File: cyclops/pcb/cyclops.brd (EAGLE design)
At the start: 124.5 x 79.9 mm, 178 parts, among them Q4 IRF510, U1 MCP4921, U11 THS4281, U12 MAX4564, U13 ZXTD, U14 ZXTD, U15 OPA1664, U2 LT1931, U3 LT1764A, U31 TPS62153, U4 BD60HC5WEFJ, U5 TPS72325, U6 LT1711, U7 TLV3701, U8 ADR03, U9 LT1880

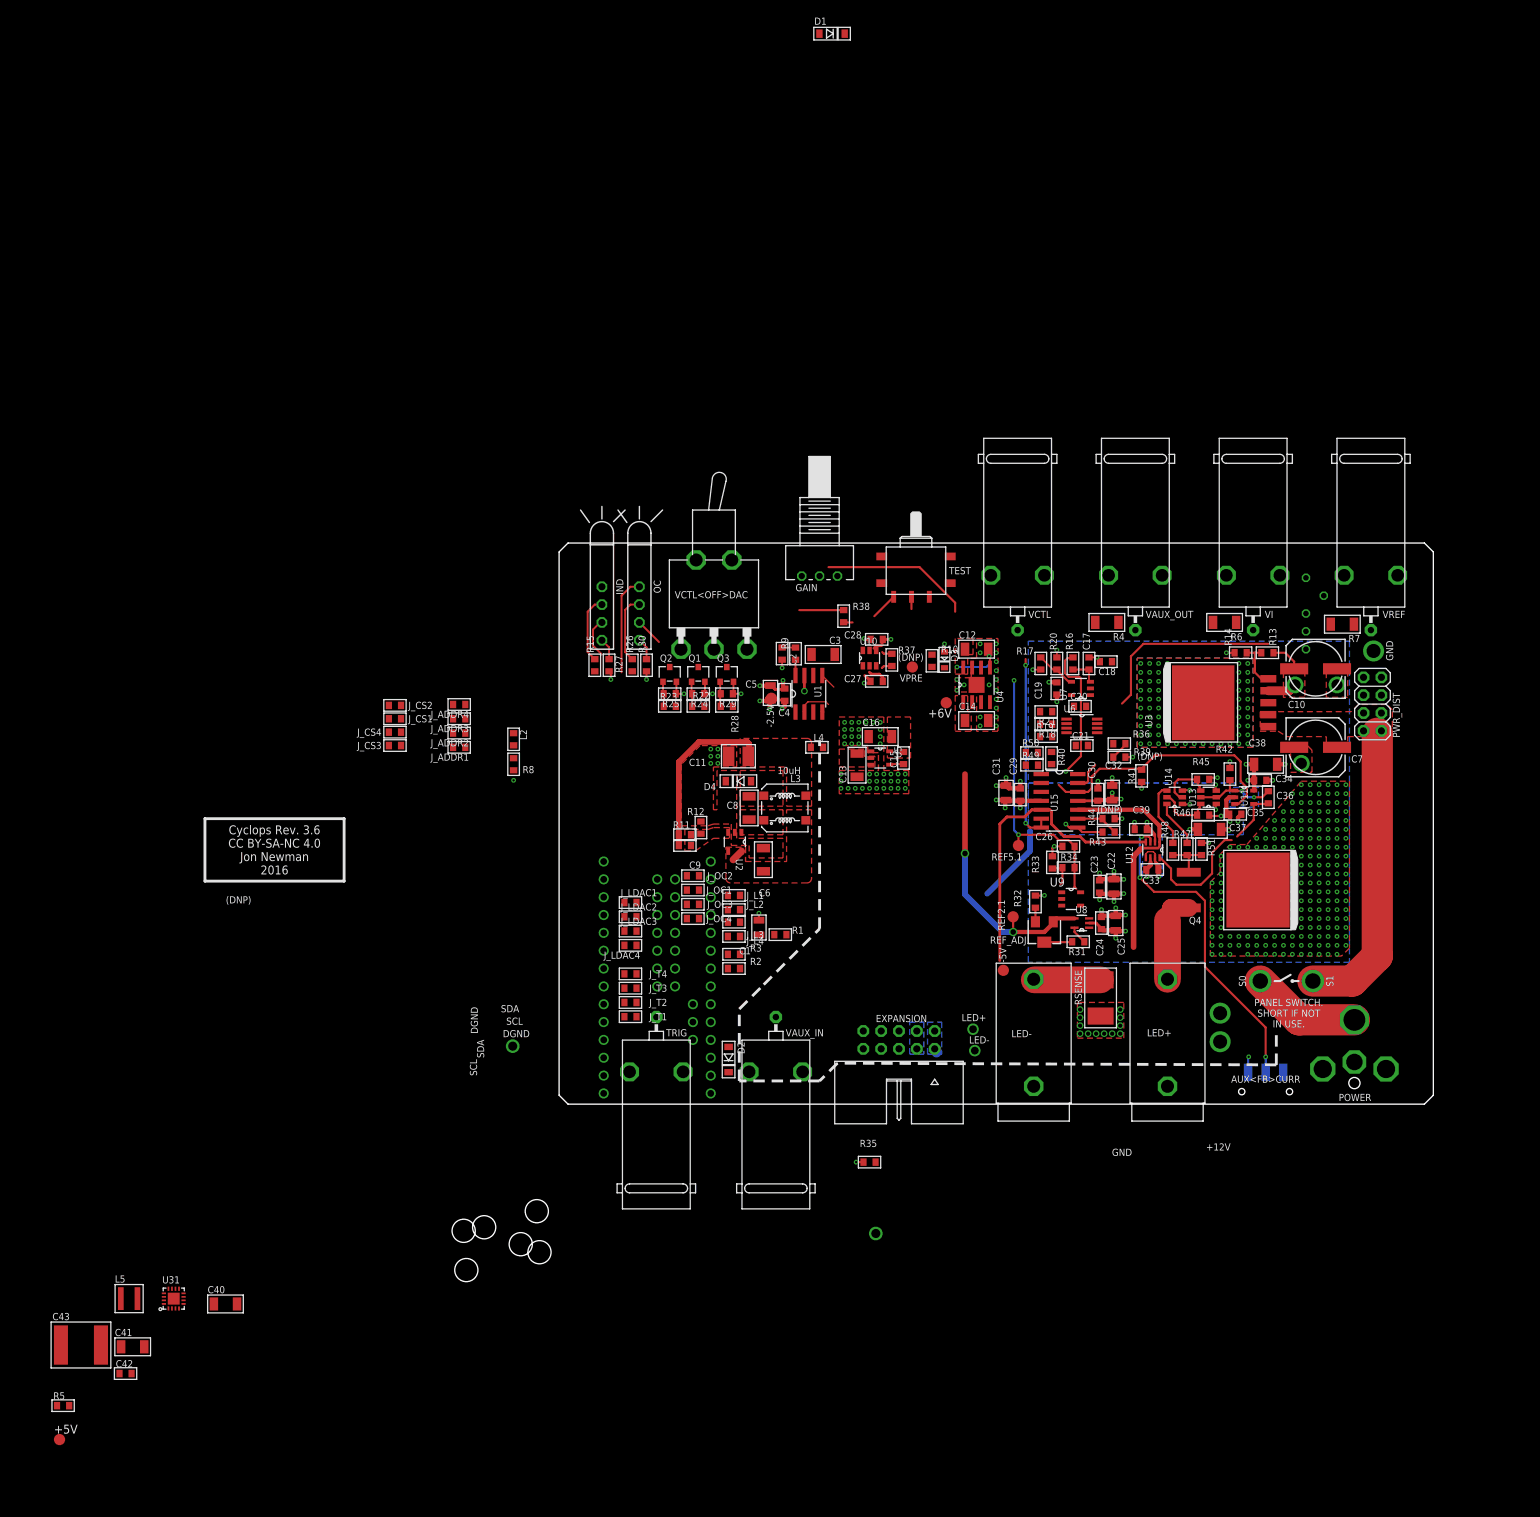
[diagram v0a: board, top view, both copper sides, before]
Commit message: Buck converter and 6V LDO added.
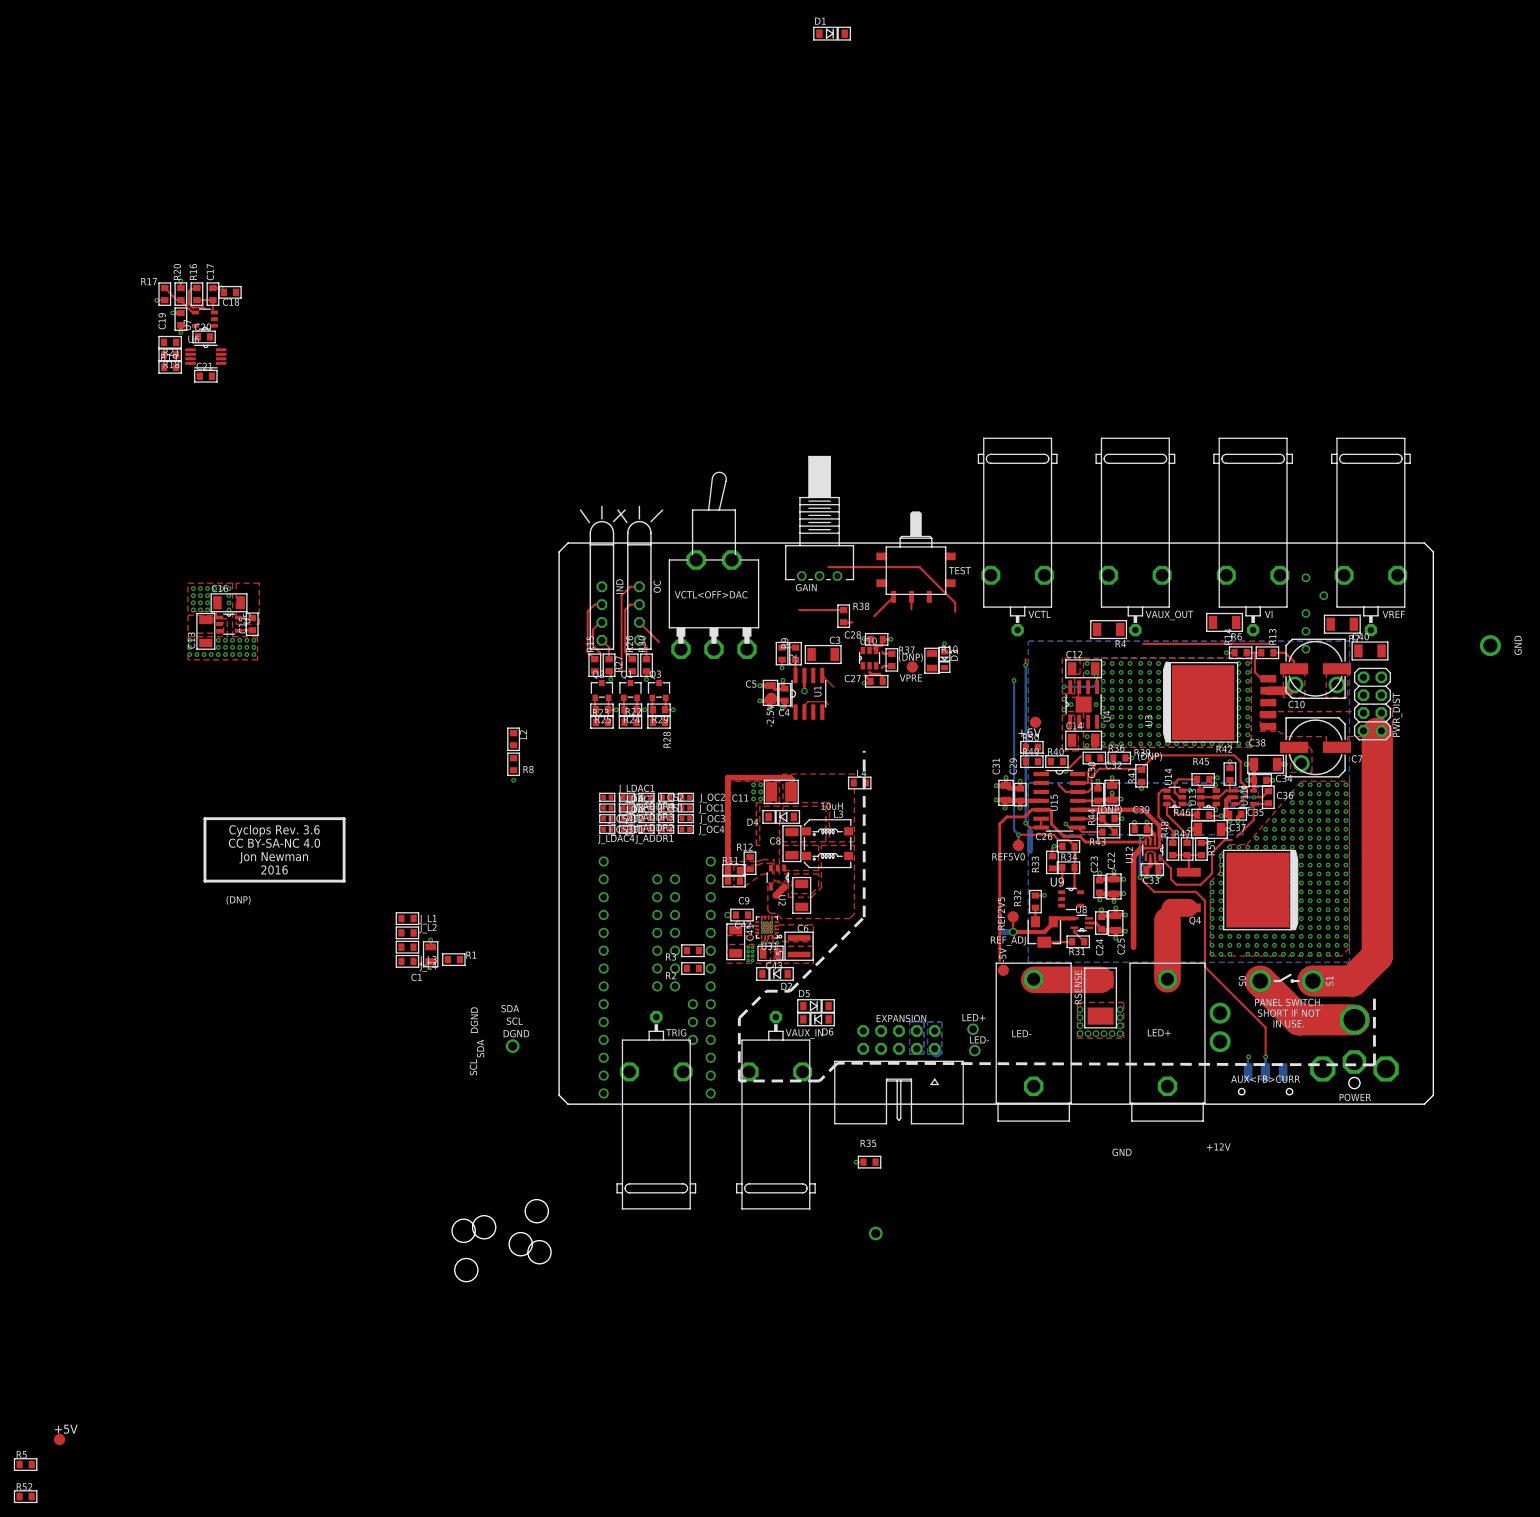
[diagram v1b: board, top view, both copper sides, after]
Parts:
- added D5, D6: STPS0560Z, jonnew:SOD123
- added R52: 4.7k, cyclops:0603
- C43: device jonnew:2220 -> jonnew:0805
- J_ADDR1, J_ADDR2, J_ADDR3, J_ADDR4, J_CS1, J_CS2, J_CS3, J_CS4, J_LDAC1, J_LDAC2, J_LDAC3, J_LDAC4, J_OC1, J_OC2, J_OC3, J_OC4, J_T1, J_T2, J_T3, J_T4: device cyclops:0603 -> jonnew:0402
- R10: device cyclops:0603 -> jonnew:0805
- R5: value 100k -> 33k
- U4: value BD60HC5WEFJ -> BD00IA5WEFJ-E2
- moved C40 187.6 mm to (115.4, 64.5)
- moved C17 135.3 mm to (-49.3, 115.3)
- moved C18 135.3 mm to (-46.9, 115.6)
- moved C19 135.3 mm to (-53.8, 111.8)
- moved C20 135.3 mm to (-50.5, 109.2)
- moved C21 135.3 mm to (-50.3, 103.6)
- moved R16 135.3 mm to (-51.6, 115.3)
- moved R17 135.3 mm to (-56.1, 115.3)
- moved R18 135.3 mm to (-55.4, 106.7)
- moved R19 135.3 mm to (-55.4, 104.9)
- moved R20 135.3 mm to (-53.8, 115.3)
- moved R21 135.3 mm to (-55.4, 108.5)
- moved U6 135.3 mm to (-50.3, 106.4)
- moved U7 135.3 mm to (-50.4, 111.8)
- moved C43 112.9 mm to (30.1, 21.5), turned to 180 degrees
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- renumbered REF2.1 to REF2V5, REF5.1 to REF5V0
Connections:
- removed net N$59: C43.2
- removed net PG: R5.1, U31.4
- removed net V+: C24.1, C25.1, U9.5
- new net N$43: R5.1, R52.2, U4.2
- net +13.3V: now also C12.1, U4.5, U4.8
- net +15V: no longer C12.1, U4.5, U4.8
- net +5V: no longer R5.2
- net +6V: now also C24.1, C25.1, R5.2, U9.5
- net GND: now also C41.2, C42.2, C43.2, R52.1, U31.7, U31.8
- net N$48: now also D6.A; no longer U31.7, U31.8
- net N$53: now also D5.C; no longer C41.2, C42.2
- net VAUX: now also D5.A, D6.C
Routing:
- net REF2.5: track 38.1 -> 13.4 mm, vias 2 -> 1
- net VI: track 32.9 -> 21.9 mm
- net VREF: track 27.7 -> 17.9 mm
- net -2.5V: track 36.7 -> 28.1 mm
- net +13.3V: track 25.2 -> 32.8 mm, vias 209 -> 211
- net +15V: track 50.0 -> 42.4 mm, vias 3 -> 1
- net +5V: track 1.68 -> 6.31 mm, vias 0 -> 2
- net V+: track 3.89 -> 0.00 mm, vias 1 -> 0
- net +6V: track 28.0 -> 31.9 mm, vias 11 -> 12
- net N$8: track 6.90 -> 4.28 mm
- net N$35: track 25.0 -> 25.8 mm
- net GND: track 66.9 -> 66.8 mm, vias 189 -> 237
- added copper zone on layer 1, net +5V
- added copper zone on layer 1, net SW
- removed copper zone on layer 1, net TEENSY_VIN

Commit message: Most digital layout is complete.
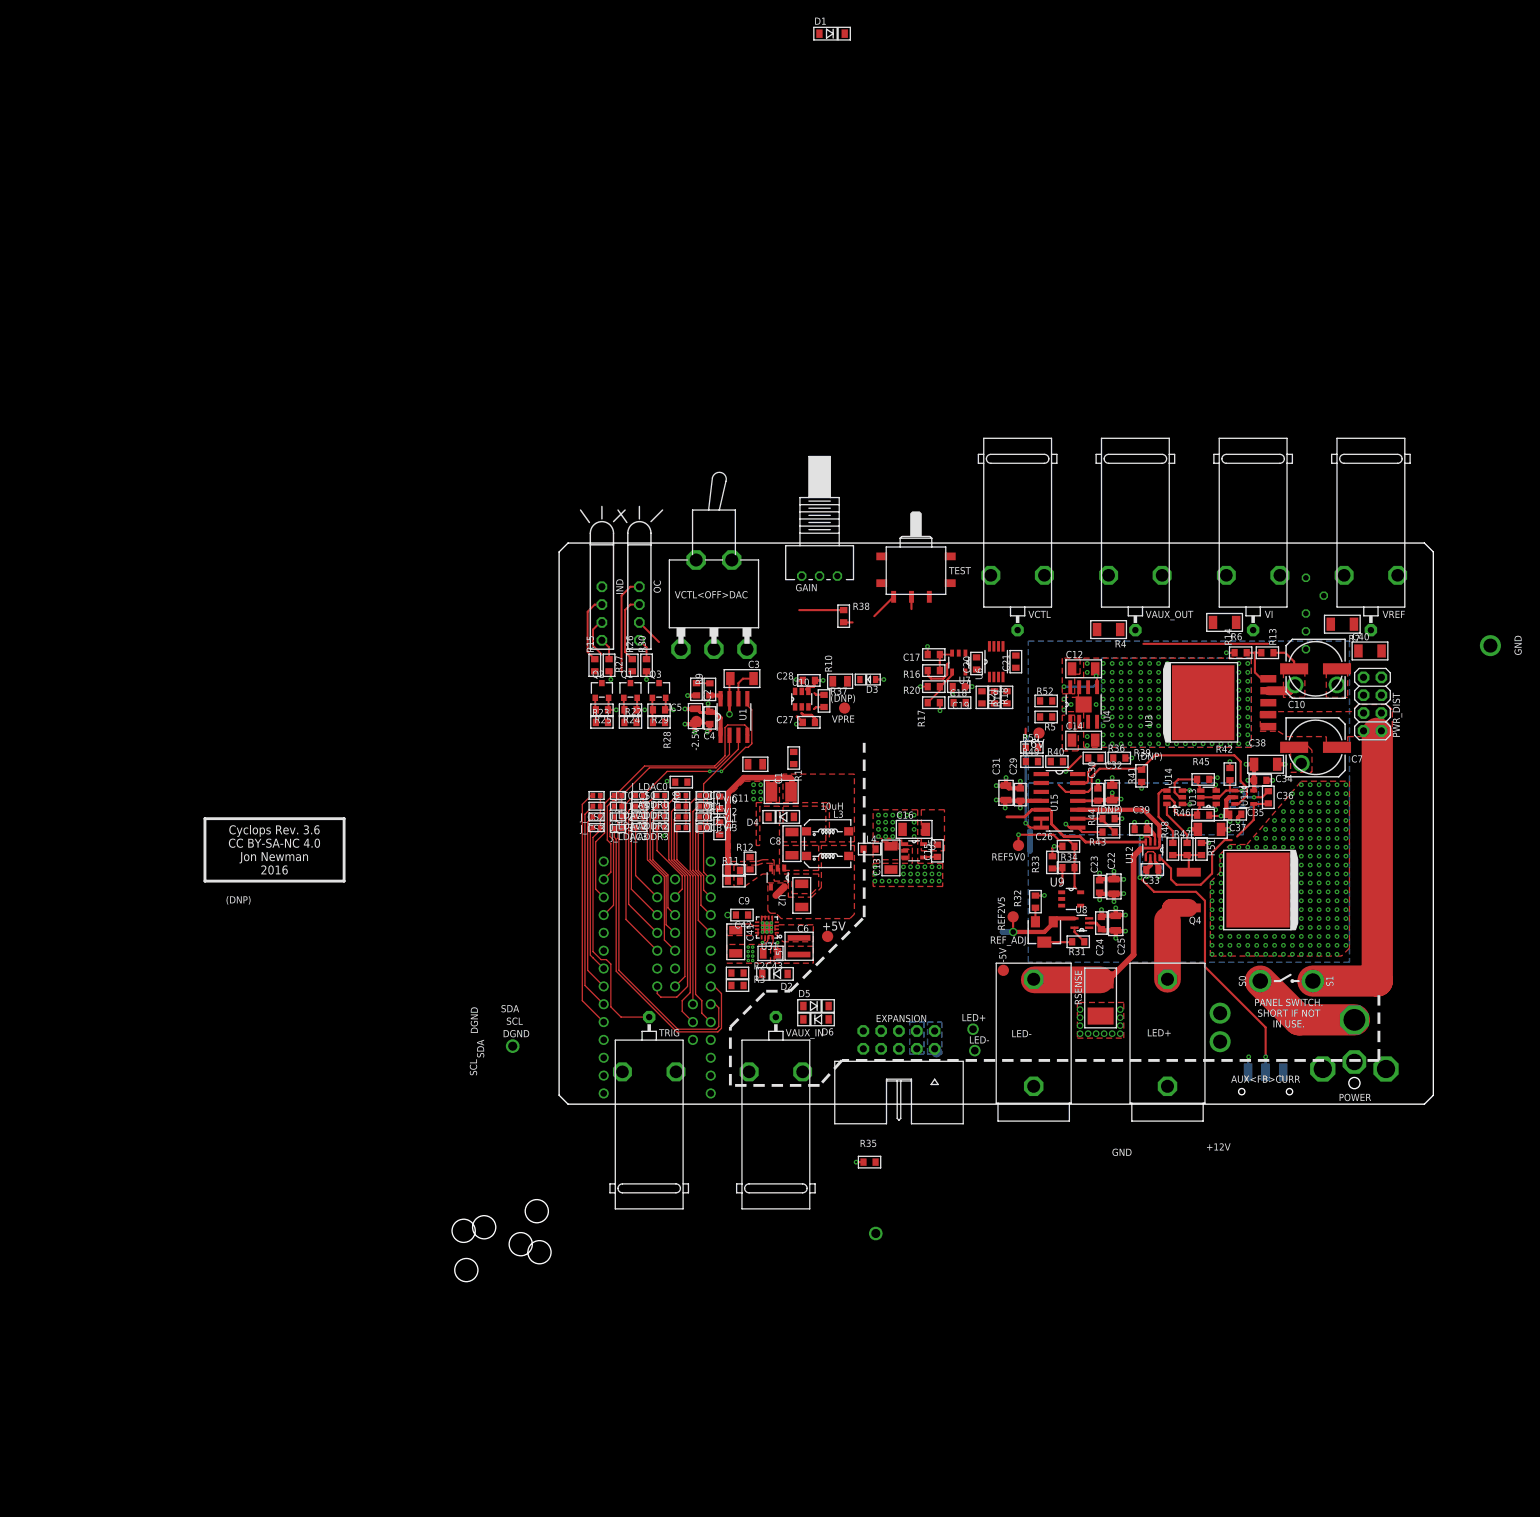
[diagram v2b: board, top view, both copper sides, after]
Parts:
- removed J_ADDR4, J_CS4, J_LDAC4, J_OC4, J_T4: 0, jonnew:0402
- removed J_L1, J_L2, J_L3, J_L4: MPZ1608, cyclops:0603
- added J_ADDR0, J_CS0, J_LDAC0, J_OC0, J_T0, J_VI0, J_VI1, J_VI2, J_VI3: 0, jonnew:0402
- added L1: MPZ1608, cyclops:0603
- moved R52 184.2 mm to (69.3, 57.4)
- moved R5 180.1 mm to (69.3, 55.1), turned to 180 degrees
- moved +5V 130.7 mm to (38.2, 23.9)
- moved R19 128.1 mm to (63.8, 57.9), turned to 90 degrees
- moved R18 127.1 mm to (62.0, 57.9), turned to 270 degrees
- moved R21 126.1 mm to (60.2, 57.9), turned to 270 degrees
- moved R17 124.0 mm to (53.3, 57.1), turned to 180 degrees
- moved C19 122.5 mm to (56.9, 59.4), turned to 180 degrees
- moved C21 122.3 mm to (65.0, 63.0), turned to 90 degrees
- moved R20 120.9 mm to (53.3, 59.4), turned to 180 degrees
- moved U6 120.6 mm to (62.2, 63.0), turned to 90 degrees
- moved C20 119.4 mm to (59.4, 62.7), turned to 90 degrees
- moved C18 119.2 mm to (57.0, 57.1), turned to 0 degrees
- moved U7 117.9 mm to (56.9, 62.9), turned to 180 degrees
- moved R16 117.8 mm to (53.3, 61.7), turned to 180 degrees
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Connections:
- removed net N$19: J_L3.1, UC.17/A3
- removed net N$21: J_L2.1, UC.16/A2
- removed net N$23: J_L1.1, UC.15/A1
- removed net N$40: J_ADDR1.2, UC.33
- removed net N$41: J_ADDR2.2, UC.32
- removed net N$44: J_ADDR3.2, UC.31
- removed net N$45: J_ADDR4.2, UC.30
- removed net N$7: J_L4.1, UC.22/A8
- new net ADDR0: J_ADDR0.2, UC.33
- new net ADDR1: J_ADDR1.2, UC.32
- new net ADDR2: J_ADDR2.2, UC.31
- new net ADDR3: J_ADDR3.2, UC.30
- new net N$58: J_VI0.2, J_VI1.2, J_VI2.2, J_VI3.2, L1.1
- new net VI0: J_VI0.1, UC.22/A8
- new net VI1: J_VI1.1, UC.17/A3
- new net VI2: J_VI2.1, UC.16/A2
- new net VI3: J_VI3.1, UC.15/A1
- net CS: now also J_CS0.1, J_CS2.2; no longer J_CS2.1, J_CS4.2
- net CS0: now also J_CS0.2; no longer J_CS2.2
- net CS2: now also J_CS2.1, UC.21/A7; no longer J_CS3.1, UC.20/A6
- net CS3: now also J_CS3.1, UC.20/A6; no longer J_CS4.1, UC.21/A7
- net GND: now also J_ADDR0.1; no longer J_ADDR4.1
- net LDAC: now also J_LDAC0.2; no longer J_LDAC4.2
- net LDAC0: now also J_LDAC0.1; no longer J_LDAC4.1
- net LDAC1: now also J_LDAC1.2; no longer J_LDAC3.2
- net LDAC3: now also J_LDAC3.2; no longer J_LDAC1.2
- net N$38: now also J_OC0.1; no longer J_OC4.1
- net OC0: now also J_OC0.2, UC.A13; no longer J_OC4.2, UC.A10
- net OC1: now also J_OC1.2, UC.A12; no longer J_OC3.2, UC.A11
- net OC2: now also UC.A10; no longer UC.A12
- net OC3: now also J_OC3.2, UC.A11; no longer J_OC1.2, UC.A13
- net OVER_CURR: now also U10.6
- net T0: now also J_T0.1; no longer J_T1.1
- net T1: now also J_T1.1; no longer J_T2.1
- net T2: now also J_T2.1; no longer J_T3.1
- net T3: now also J_T3.1; no longer J_T4.1
- net TRIG: now also J_T0.2; no longer J_T4.2
- net VI_LP: now also L1.2; no longer J_L1.2, J_L2.2, J_L3.2, J_L4.2
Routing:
- net CS3: track 0.00 -> 46.2 mm
- net CS2: track 0.00 -> 44.0 mm
- net MOSI: track 0.50 -> 40.4 mm
- net TRIG: track 0.00 -> 38.1 mm
- net T0: track 0.00 -> 34.3 mm
- net VI0: track 0.00 -> 34.2 mm
- net OC1: track 0.00 -> 33.3 mm
- net OC2: track 0.00 -> 31.6 mm
- net T1: track 0.00 -> 29.8 mm
- net OC0: track 0.00 -> 29.4 mm
- net LDAC: track 2.33 -> 29.8 mm, vias 0 -> 2
- net OC3: track 0.00 -> 26.2 mm
- net T2: track 0.00 -> 25.4 mm
- net LDAC0: track 0.00 -> 24.6 mm
- net ADDR0: track 0.00 -> 24.4 mm
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- added copper zone on layer 15, net +5V
- added copper zone on layer 2, net NOGND

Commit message: Almost done with layout.
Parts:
- R10: device jonnew:0805 -> jonnew:0603
- R15: value 3k -> 2.2k
- moved -2.5V 49.9 mm to (61.7, 27.8)
- moved REF_ADJ 38.8 mm to (56.1, 61.1), turned to 90 degrees
- moved R31 38.3 mm to (54.7, 56.3), turned to 270 degrees
- moved REF2V5 38.1 mm to (58.3, 64.3), turned to 0 degrees
- moved U8 34.5 mm to (57.4, 55.8), turned to 90 degrees
- moved R32 34.3 mm to (60.5, 62.4), turned to 180 degrees
- moved C24 33.6 mm to (57.4, 53.0), turned to 180 degrees
- moved C25 33.3 mm to (57.4, 50.9), turned to 180 degrees
- moved U9 30.6 mm to (60.8, 57.3), turned to 270 degrees
- moved R34 28.3 mm to (63.4, 60.5), turned to 270 degrees
- moved C23 27.2 mm to (62.7, 54.2), turned to 0 degrees
- moved C22 26.7 mm to (62.7, 52.2), turned to 0 degrees
- moved R33 23.5 mm to (63.4, 56.9), turned to 270 degrees
- moved C21 22.7 mm to (48.3, 47.8), turned to 270 degrees
- moved R16 21.4 mm to (32.3, 58.3), turned to 0 degrees
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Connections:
- removed net N$38: J_OC0.1, J_OC1.1, J_OC2.1, J_OC3.1, L2.2, R8.1
- removed net V-: R20.2, U7.2, U9.2
- new net OVER_CURR_PRE: J_OC0.1, J_OC1.1, J_OC2.1, J_OC3.1, L2.2, R28.2, R8.1
- net GND: now also R20.2, U7.2, U9.2
- net OVER_CURR: no longer R28.2
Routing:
- net VINPUT: track 0.00 -> 57.5 mm
- net OVER_CURR_PRE: track 0.00 -> 44.7 mm, vias 0 -> 4
- net N$27: track 0.00 -> 36.0 mm
- net N$34: track 3.89 -> 32.4 mm
- net N$37: track 0.00 -> 27.3 mm
- net GND: track 74.8 -> 99.7 mm, vias 237 -> 260
- net +6V: track 36.2 -> 56.0 mm, vias 12 -> 22
- net VCTL_PROTECT: track 6.32 -> 24.2 mm
- net N$14: track 2.75 -> 16.7 mm
- net N$42: track 0.00 -> 13.0 mm
- net N$58: track 4.57 -> 16.3 mm
- net DACA: track 1.99 -> 10.5 mm
- net +15V: track 44.5 -> 51.7 mm, vias 1 -> 3
- net N$50: track 0.00 -> 7.22 mm
- net -2.5V: track 28.1 -> 34.6 mm, vias 9 -> 27
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- added copper zone on layer 15, net +15V
